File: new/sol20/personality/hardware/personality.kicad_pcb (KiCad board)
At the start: 2 copper layers, 44.4 x 96.5 mm, 8 parts, among them J1 Personality-connector, U1 74LS08, U2 28C256

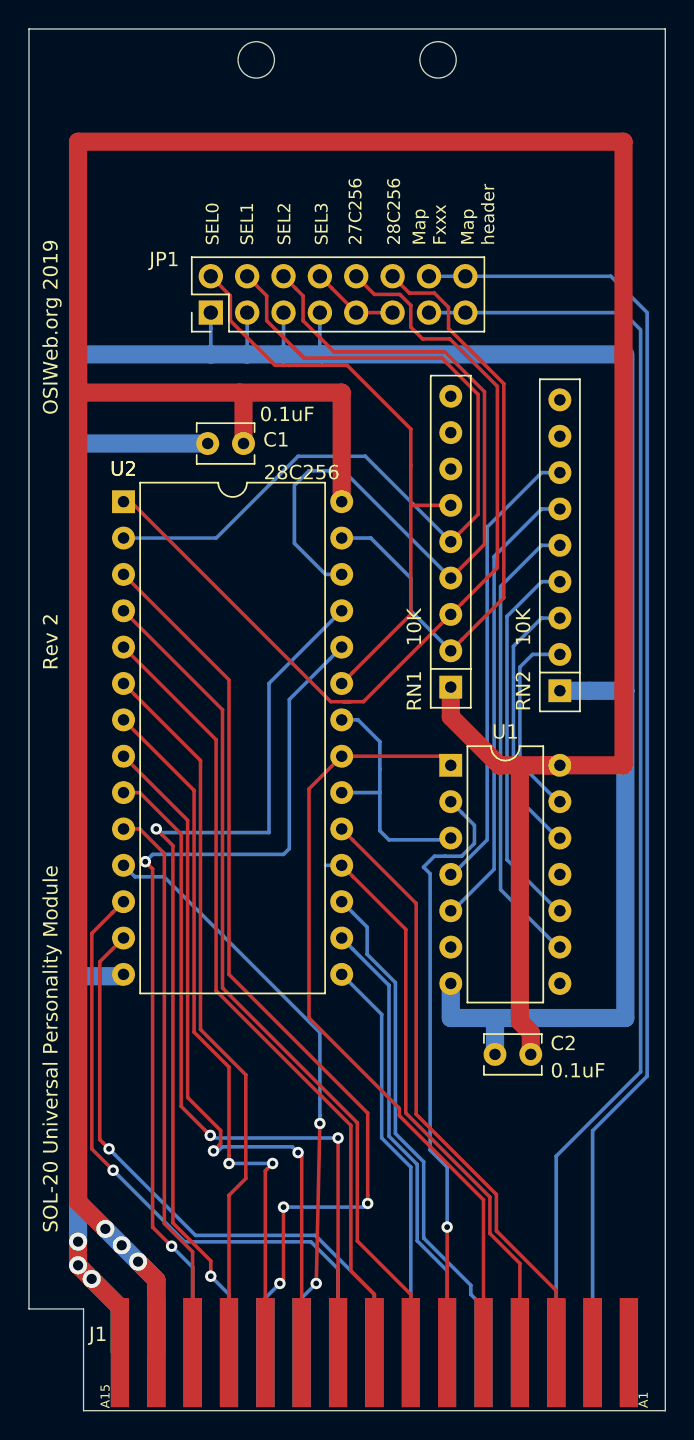
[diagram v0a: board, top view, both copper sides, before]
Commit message: Board outline cleanup
- round the corners of the edge connector
- consolidate outline into polygon.
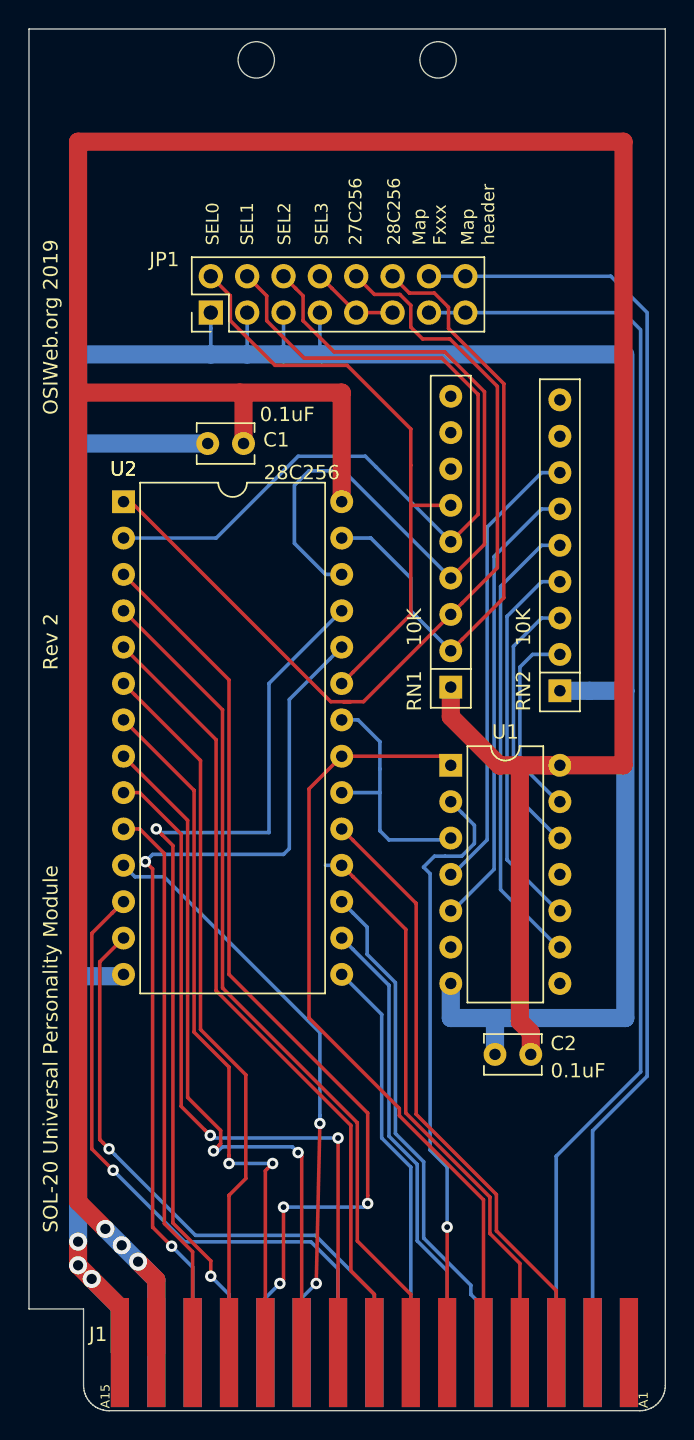
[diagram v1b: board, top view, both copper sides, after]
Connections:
- net /~C0 renamed /~{C0}
- net /~C4 renamed /~{C4}
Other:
- outline, holes or cut-outs redrawn
- net class Default removed
- net class Power removed

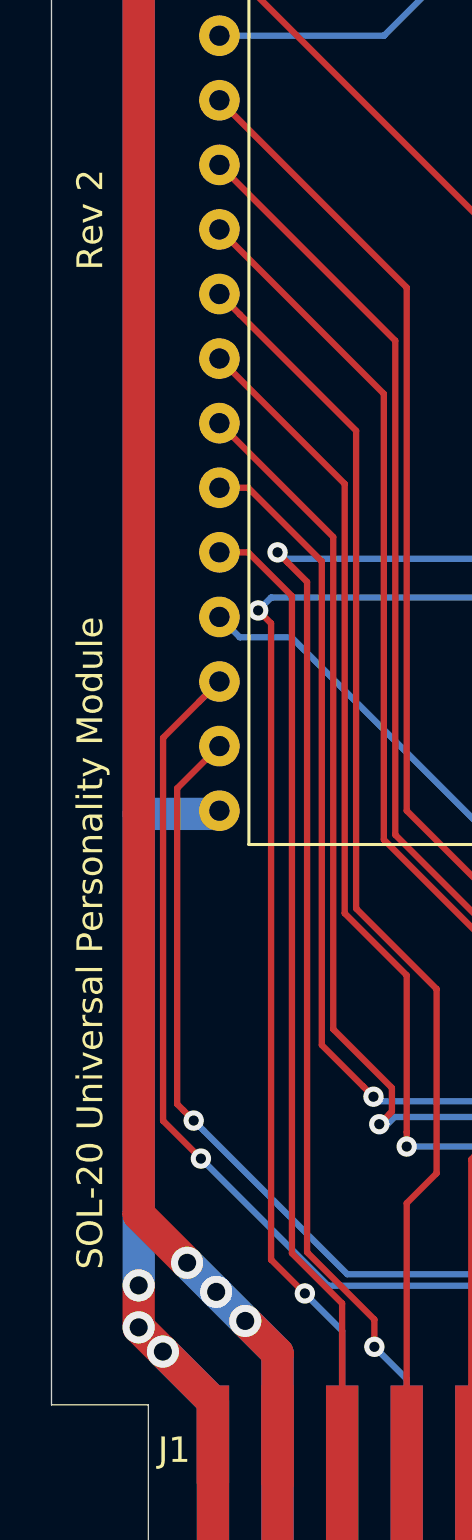
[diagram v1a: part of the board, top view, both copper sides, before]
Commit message: Update to kicad v6
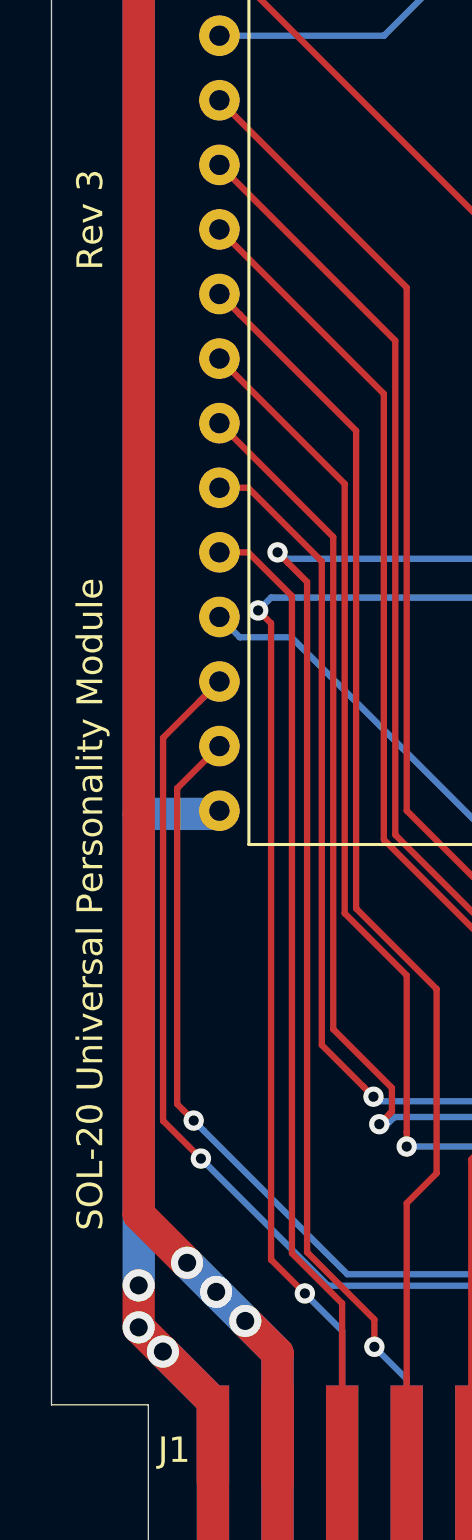
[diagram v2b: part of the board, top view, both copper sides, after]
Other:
- board text added: "${TITLE}"
- board text added: "Rev ${REVISION}"
- board text removed: "Rev 2"
- board text removed: "SOL-20 Universal Personality Module"
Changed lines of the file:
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@@
   )
   (paper "A4")
+  (title_block
+    (title "SOL-20 Universal Personality Module")
+    (date "2022-10-11")
+    (rev "3")
+    (company "OSIWeb.org")
+  )
   (layers
     (0 "F.Cu" signal)
@@
       (xy 119.126 140.97)
     ) (layer "Edge.Cuts") (width 0.05) (fill none))
-  (gr_text "Rev 2\n" (at 116.84 94.361 90) (layer "F.SilkS")
+  (gr_text "Rev ${REVISION}\n" (at 116.84 94.361 90) (layer "F.SilkS")
     (effects (font (size 1.016 1.016) (thickness 0.1016)))
   )
@@
     (effects (font (size 1.016 1.016) (thickness 0.1016)))
   )
-  (gr_text "SOL-20 Universal Personality Module" (at 116.84 122.809 90) (layer "F.SilkS")
+  (gr_text "${TITLE}" (at 116.84 121.285 90) (layer "F.SilkS")
     (effects (font (size 1.016 1.016) (thickness 0.1016)))
   )
